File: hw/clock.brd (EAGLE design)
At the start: 98.7 x 80 mm, 46 parts, among them IC1 AT90S2313S, IC2 PCF2123TSSOP14, Q1 BSS84, Q2 BSS84, Q3 BSS84, Q4 BSS84, U1 TLC59282_DBQ_24, X1 4MHz, X2 CRYSTALTFORK_SMD

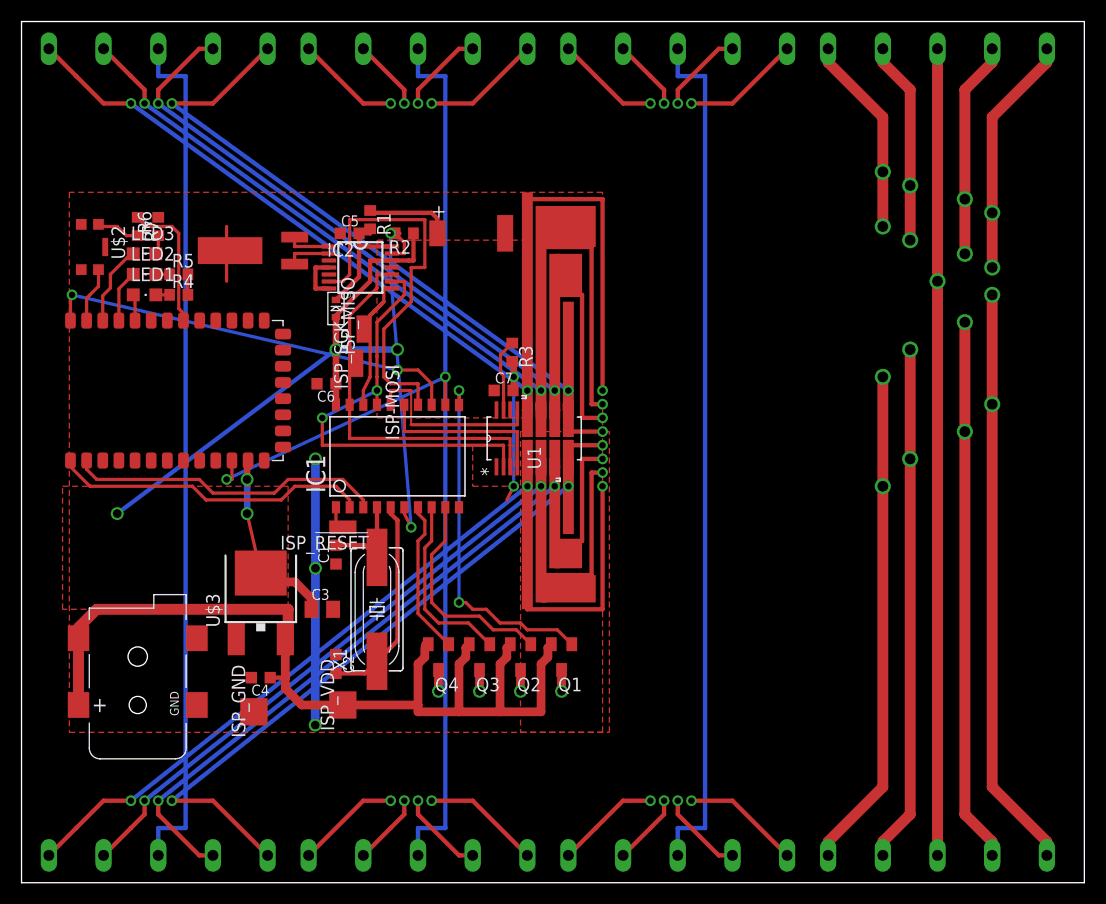
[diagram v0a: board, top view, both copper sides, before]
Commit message: Fix reversed SPI lines, remove superfluous pull-up on RTC.CLKOUT, improve vias.
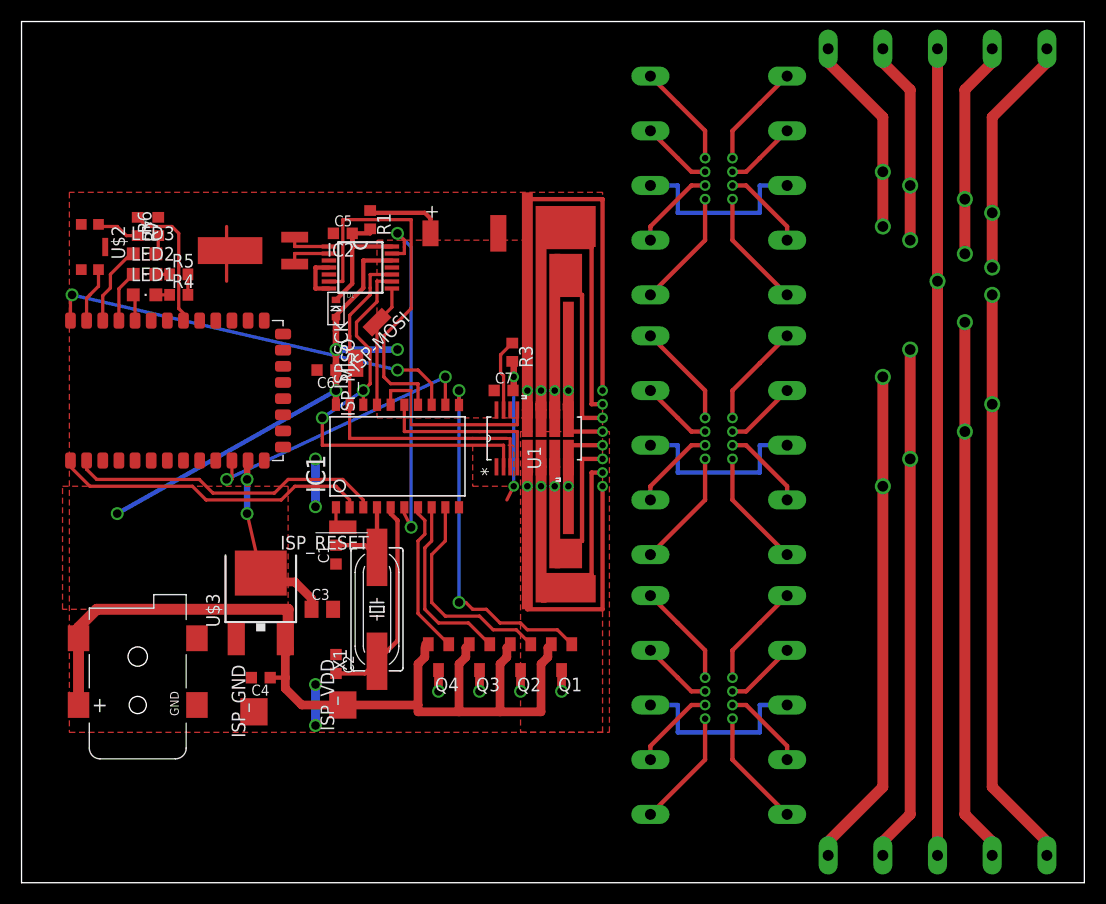
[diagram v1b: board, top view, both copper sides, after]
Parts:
- removed R2: 10k, rcl:R0603
- ISP-MOSI: value WIREPADSMDCONTACT -> WIREPADSMD1,27-254; device jocki:SMDCONTACT -> jocki:SMD1,27-2,54
- ISP_MISO: value WIREPADSMD1,27-254 -> WIREPADSMDCONTACT; device jocki:SMD1,27-2,54 -> jocki:SMDCONTACT
- moved DISP4BOT 77.2 mm to (58.4, 64.8), turned to 270 degrees
- moved DISP2TOP 61.8 mm to (71.1, 16.5), turned to 90 degrees
- moved DISP4TOP 59.8 mm to (71.1, 64.8), turned to 90 degrees
- moved DISP3TOP 50.3 mm to (71.1, 40.6), turned to 90 degrees
- moved DISP3BOT 43.8 mm to (58.4, 40.6), turned to 270 degrees
- moved DISP2BOT 14.2 mm to (58.4, 16.5), turned to 270 degrees
- moved ISP-MOSI 6.35 mm to (33.0, 52.1), turned to 135 degrees
- moved ISP_MISO 5.72 mm to (31.8, 45.7)
- moved C6 1.27 mm to (28.3, 47.6)
- moved C5 0.64 mm to (29.8, 60.3)
- moved C8 0.63 mm to (40.6, 60.3)
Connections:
- removed net MISO: IC1.18, IC2.8, ISP_MISO.1
- removed net MOSI: IC1.17, IC2.9, ISP-MOSI.1, U1.2
- new net MISO/DO: IC1.18, IC2.9, ISP_MISO.1, U1.2
- new net MOSI/DI: IC1.17, IC2.8, ISP-MOSI.1
- net +3V3: no longer R2.1
- net 1HZ: no longer R2.2
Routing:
- net ANODE4: track 82.0 -> 19.8 mm
- net ANODE3: track 82.0 -> 19.8 mm
- net ANODE2: track 82.0 -> 19.8 mm
- net D: track 141.0 -> 94.0 mm
- net C: track 141.0 -> 94.0 mm
- net DP: track 143.3 -> 96.3 mm
- net E: track 155.6 -> 108.6 mm
- net G: track 138.3 -> 92.8 mm
- net F: track 120.9 -> 75.5 mm
- net A: track 116.6 -> 71.1 mm
- net B: track 109.1 -> 63.6 mm
- net MOSI: track 40.7 -> 0.00 mm, vias 2 -> 0
- net MISO/DO: track 0.00 -> 40.4 mm, vias 0 -> 2
- net MISO: track 18.7 -> 0.00 mm
- net GND: track 50.5 -> 34.1 mm, vias 5 -> 6
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
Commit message: Connect button to BT module's AT_ENABLE pin
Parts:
- removed R7: 10K, rcl:R0603
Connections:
- removed net N$11: R7.2, U$1.P$33, U$2.A1, U$2.A2
- removed net N$20: R7.1, U$1.P$27
- net N$8: now also U$2.A1, U$2.A2
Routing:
- net N$20: track 13.1 -> 0.00 mm
- net N$11: track 9.27 -> 0.00 mm
- net N$8: track 39.2 -> 43.6 mm
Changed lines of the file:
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@@
 <rectangle x1="38.1" y1="58.42" x2="43.18" y2="62.23" layer="41" rot="R180"/>
 <dimension x1="85.09" y1="2.54" x2="85.09" y2="55.88" x3="73.66" y3="29.21" textsize="1.778" layer="51" unit="inch"/>
+<rectangle x1="4" y1="39.5" x2="24" y2="52" layer="41"/>
 </plain>
 <attributes>
@@
 <element name="R5" library="rcl" package="R0603" value="470" x="14.605" y="56.515"/>
 <element name="R6" library="rcl" package="R0603" value="100" x="12.7" y="60.96" rot="R90"/>
-<element name="R7" library="rcl" package="R0603" value="10K" x="10.795" y="60.96" rot="R270"/>
 <element name="C6" library="rcl" package="C0603K" value="100n" x="28.325" y="47.625" rot="R180"/>
 <element name="C7" library="rcl" package="C0603K" value="100n" x="44.7802" y="45.73"/>
@@
 <wire x1="4.695" y1="54.61" x2="4.545" y2="54.61" width="0.3048" layer="1"/>
 <wire x1="4.545" y1="54.61" x2="4.545" y2="52.22" width="0.3048" layer="1"/>
+<contactref element="U$2" pad="A1"/>
+<contactref element="U$2" pad="A2"/>
+<wire x1="4.695" y1="54.61" x2="6.35" y2="54.61" width="0.3048" layer="1"/>
+<wire x1="6.35" y1="54.61" x2="6.985" y2="55.245" width="0.3048" layer="1"/>
+<wire x1="6.985" y1="55.245" x2="7.15" y2="55.41" width="0.3048" layer="1"/>
+<wire x1="7.15" y1="55.41" x2="7.15" y2="56.955" width="0.3048" layer="1"/>
+<wire x1="7.15" y1="56.955" x2="7.15" y2="61.155" width="0" layer="19" extent="1-1"/>
 </signal>
 <signal name="N$10">
@@
 <wire x1="19.545" y1="37.465" x2="19.545" y2="39.22" width="0.3048" layer="1"/>
 </signal>
-<signal name="N$11">
-<contactref element="U$1" pad="P$33"/>
-<contactref element="R7" pad="2"/>
-<contactref element="U$2" pad="A1"/>
-<contactref element="U$2" pad="A2"/>
-<wire x1="7.15" y1="56.955" x2="7.15" y2="55.41" width="0.3048" layer="1"/>
-<wire x1="7.15" y1="55.41" x2="6.35" y2="54.61" width="0.3048" layer="1"/>
-<wire x1="6.35" y1="54.61" x2="6.045" y2="54.305" width="0.3048" layer="1"/>
-<wire x1="6.045" y1="54.305" x2="6.045" y2="52.22" width="0.3048" layer="1"/>
-<wire x1="7.15" y1="61.155" x2="7.345" y2="60.96" width="0.3048" layer="1"/>
-<wire x1="7.345" y1="60.96" x2="8.89" y2="60.96" width="0.3048" layer="1"/>
-<wire x1="8.89" y1="60.96" x2="9.74" y2="60.11" width="0.3048" layer="1"/>
-<wire x1="9.74" y1="60.11" x2="10.795" y2="60.11" width="0.3048" layer="1"/>
-<wire x1="7.15" y1="56.955" x2="7.345" y2="60.96" width="0" layer="19" extent="1-1"/>
-</signal>
 <signal name="N$13">
 <contactref element="R4" pad="1"/>
@@
 <wire x1="29.21" y1="33.02" x2="29.21" y2="34.8742" width="0.3048" layer="1"/>
 </signal>
-<signal name="N$20">
-<contactref element="R7" pad="1"/>
-<contactref element="U$1" pad="P$27"/>
-<wire x1="15.24" y1="52.415" x2="15.045" y2="52.22" width="0.3048" layer="1"/>
-<wire x1="10.795" y1="61.81" x2="11.645" y2="60.96" width="0.3048" layer="1"/>
-<wire x1="11.645" y1="60.96" x2="13.97" y2="60.96" width="0.3048" layer="1"/>
-<wire x1="13.97" y1="60.96" x2="14.605" y2="60.325" width="0.3048" layer="1"/>
-<wire x1="14.605" y1="60.325" x2="14.605" y2="57.15" width="0.3048" layer="1"/>
-<wire x1="14.605" y1="57.15" x2="14.605" y2="53.34" width="0.3048" layer="1"/>
-<wire x1="14.605" y1="53.34" x2="15.24" y2="52.705" width="0.3048" layer="1"/>
-<wire x1="15.24" y1="52.705" x2="15.24" y2="52.415" width="0.3048" layer="1"/>
-<wire x1="15.24" y1="52.415" x2="15.045" y2="52.22" width="0.3048" layer="1"/>
-</signal>
 <signal name="MISO/DO">

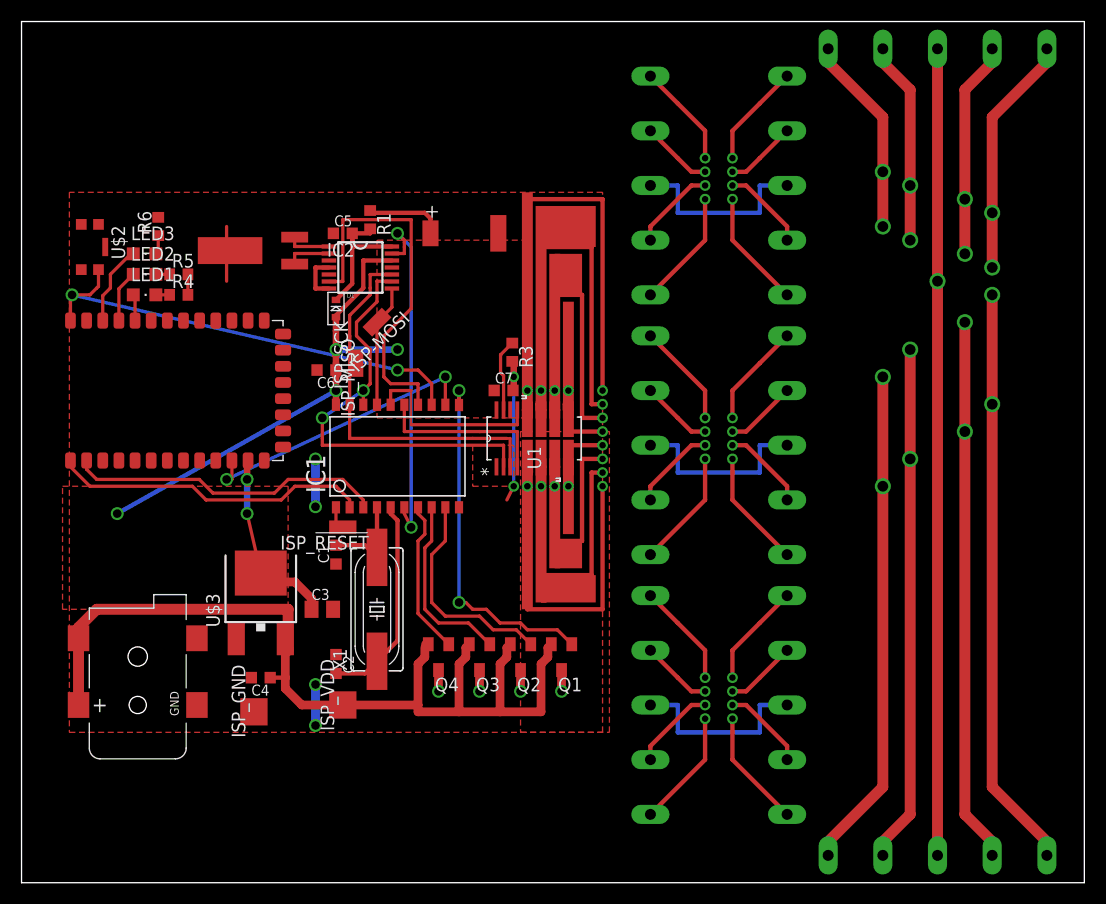
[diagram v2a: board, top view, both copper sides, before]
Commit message: HW v2.0, with proper level shifters
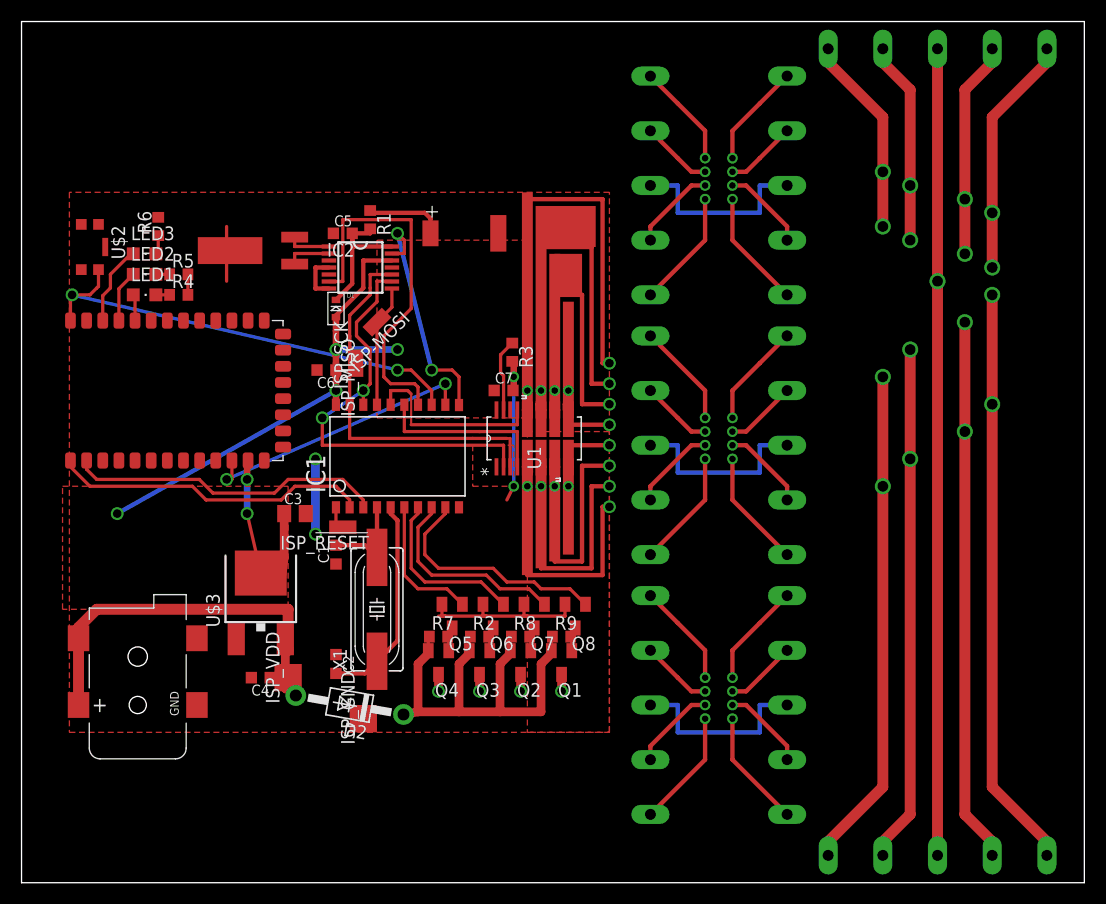
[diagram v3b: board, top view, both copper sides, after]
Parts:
- added D2: 1N4004, adafruit:DO41-10
- added Q5, Q6, Q7, Q8: BSS123, transistor-small-signal:SOT23
- added R2, R7, R8, R9: 500R, rcl:R0603
- moved ISP_GND 10.2 mm to (31.8, 15.2)
- moved C3 9.25 mm to (25.4, 34.3)
- moved ISP_VDD 5.68 mm to (24.8, 19.1)
- moved Q1 0.50 mm to (50.2, 20.5)
- moved Q2 0.50 mm to (46.4, 20.5)
- moved Q3 0.50 mm to (42.5, 20.5)
- moved Q4 0.50 mm to (38.7, 20.5)
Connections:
- new net N$11: D2.C, Q1.2, Q2.2, Q3.2, Q4.2, R2.1, R7.1, R8.1, R9.1
- new net N$28: Q1.1, Q8.3, R9.2
- new net N$29: Q2.1, Q7.3, R8.2
- new net N$30: Q3.1, Q6.3, R2.2
- new net N$31: Q4.1, Q5.3, R7.2
- net +12V: now also D2.A; no longer Q1.2, Q2.2, Q3.2, Q4.2
- net 1HZ: now also IC1.11; no longer IC1.6
- net GND: now also Q5.2, Q6.2, Q7.2, Q8.2
- net SEG1: now also IC1.6, Q5.1; no longer IC1.7, Q4.1
- net SEG2: now also IC1.7, Q6.1; no longer IC1.8, Q3.1
- net SEG3: now also IC1.8, Q7.1; no longer IC1.9, Q2.1
- net SEG4: now also IC1.9, Q8.1; no longer IC1.11, Q1.1
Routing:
- net +12V: track 89.6 -> 39.7 mm
- net N$11: track 0.00 -> 42.5 mm
- net GND: track 34.1 -> 49.9 mm, vias 6 -> 4
- net 1HZ: track 33.1 -> 21.8 mm
- net SEG4: track 33.1 -> 22.0 mm, vias 2 -> 0
- net E: track 108.6 -> 100.9 mm
- net C: track 94.0 -> 97.8 mm
- net N$31: track 0.00 -> 2.33 mm
- net N$29: track 0.00 -> 2.33 mm
- net N$28: track 0.00 -> 2.33 mm
- net N$30: track 0.00 -> 2.33 mm
- net +3V3: track 65.7 -> 67.6 mm
- net G: track 92.8 -> 90.9 mm
- net D: track 94.0 -> 92.1 mm
- net SEG1: track 14.4 -> 12.8 mm
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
